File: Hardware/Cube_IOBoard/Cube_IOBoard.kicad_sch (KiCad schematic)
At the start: 15 parts, among them J1 SPKT, J10 Pixhawk_Cube_DF17_Module_Bus_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, J11 GPS1 & I2C1, J12 GPS2 & I2C2, J13 TELEM2, J2 USB, LED & BUZZER, J4 ADC, J5 CAN2, J6 I2C2, J7 TELEM1, J8 CAN1

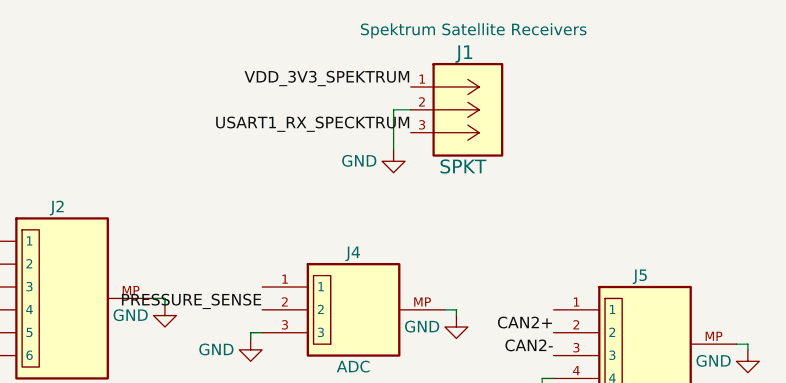
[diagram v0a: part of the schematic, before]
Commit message: Corrected some schematic symbols
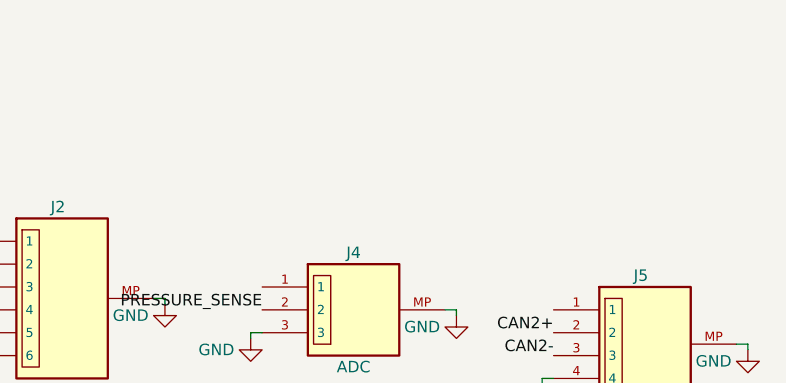
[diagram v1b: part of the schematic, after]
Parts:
- removed J1: SPKT, Connector_JST:JST_XH_B3B-XH-A_1x03_P2.50mm_Vertical, symbol 2022-11-05_21-49-56:S3B-ZR-SM4A-TFLFSN
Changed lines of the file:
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@@
-    (stroke (width 0) (type default) (color 0 0 0 0))
-  )
-  (wire (pts (xy 240.03 26.67) (xy 241.935 26.67))
     (stroke (width 0) (type default) (color 0 0 0 0))
   )
@@
     (stroke (width 0) (type default) (color 0 0 0 0))
   )
-  (wire (pts (xy 240.03 31.115) (xy 240.03 26.67))
-    (stroke (width 0) (type default) (color 0 0 0 0))
-  )
   (wire (pts (xy 224.155 51.435) (xy 224.155 52.07))
     (stroke (width 0) (type default) (color 0 0 0 0))
@@
     (effects (font (size 1.27 1.27)) (justify left bottom))
   )
-  (label "USART1_RX_SPECKTRUM" (at 241.935 29.21 180)
-    (effects (font (size 1.27 1.27)) (justify right bottom))
-  )
   (label "I2C2_SDA" (at 225.425 98.425 180)
     (effects (font (size 1.27 1.27)) (justify right bottom))
@@
   )
   (label "SAFETY" (at 87.63 48.26 180)
-    (effects (font (size 1.27 1.27)) (justify right bottom))
-  )
-  (label "VDD_3V3_SPEKTRUM" (at 241.935 24.13 180)
     (effects (font (size 1.27 1.27)) (justify right bottom))
   )
@@
     )
     (property "Datasheet" "~" (id 3) (at 222.885 136.525 0)
-      (effects (font (size 1.27 1.27)) hide)
-    )
-    (pin "1")
-  )
-  (symbol (lib_id "power:GND") (at 240.03 31.115 0) (unit 1)
-    (in_bom yes) (on_board yes)
-    (property "Reference" "#PWR01" (id 0) (at 240.03 37.465 0)
-      (effects (font (size 1.27 1.27)) hide)
-    )
-    (property "Value" "GND" (id 1) (at 236.22 32.385 0))
-    (property "Footprint" "" (id 2) (at 240.03 31.115 0)
-      (effects (font (size 1.27 1.27)) hide)
-    )
-    (property "Datasheet" "" (id 3) (at 240.03 31.115 0)
       (effects (font (size 1.27 1.27)) hide)
     )
@@
     (pin "1")
   )
-  (symbol (lib_id "2022-11-05_21-49-56:S3B-ZR-SM4A-TFLFSN") (at 239.395 24.13 0) (unit 1)
-    (in_bom yes) (on_board yes)
-    (property "Reference" "J1" (id 0) (at 247.015 20.32 0)
-      (effects (font (size 1.524 1.524)) (justify left))
-    )
-    (property "Value" "SPKT" (id 1) (at 245.11 33.02 0)
-      (effects (font (size 1.524 1.524)) (justify left))
-    )
-    (property "Footprint" "Connector_JST:JST_XH_B3B-XH-A_1x03_P2.50mm_Vertical" (id 2) (at 248.285 21.209 0)
-      (effects (font (size 1.524 1.524)) hide)
-    )
-    (property "Datasheet" "" (id 3) (at 239.395 24.13 0)
-      (effects (font (size 1.524 1.524)))
-    )
-    (property "Description" "Spektrum Satellite Receivers" (id 4) (at 248.92 17.78 0))
-    (pin "1")
-    (pin "2")
-    (pin "3")
-  )
   (symbol (lib_id "BM06B-GHS-TBT_LF__SN__N_:BM06B-GHS-TBT(LF)(SN)(N)") (at 203.2 48.895 0) (unit 1)
     (in_bom yes) (on_board yes)
@@
   )
   (symbol_instances
-    (path "/3dd67373-3ec1-4498-8b23-e797c8947129"
-      (reference "#PWR01") (unit 1) (value "GND") (footprint "")
-    )
     (path "/1dbe8a2e-d3a2-4600-97aa-34c3431dfd48"
       (reference "#PWR02") (unit 1) (value "GND") (footprint "")
@@
       (reference "H4") (unit 1) (value "MountingHole_Pad") (footprint "MountingHole:MountingHole_3.2mm_M3_DIN965_Pad")
     )
-    (path "/b492e4a1-4be3-4440-a10d-9a7c36235ae4"
-      (reference "J1") (unit 1) (value "SPKT") (footprint "Connector_JST:JST_XH_B3B-XH-A_1x03_P2.50mm_Vertical")
-    )
     (path "/b6437e22-8d20-497b-9247-f69a7a68905f"

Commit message: Added EMI filters and TVS to IO schematic, experimenting with spice sims
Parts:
- added C1, C2, C3, C4, C5, C6, C7, C8, C9: KNH16C104DA5TS, libraries:KNH16C104DA5TS, symbol Device:Filter_EMI_C
- added D1, D2, D3, D4, D5, D6, D7, D8, D9: PESD0402-140, Diode_SMD:D_0402_1005Metric, symbol Device:D_TVS
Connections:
- net GND: now also C1.2, C2.2, C3.2, C4.2, C5.2, C6.2, C7.2, C8.2, C9.2, D1.1 (A1), D2.1 (A1), D3.1 (A1), D4.1 (A1), D5.1 (A1), D6.1 (A1), D7.1 (A1), D8.1 (A1), D9.1 (A1)
- net VBUS: now also J10.29 (VBUS); no longer J2.1
- net at J8.1: now also C8.3, D8.2 (A2)
- net at J4.1: now also C1.3, D1.2 (A2)
- net at J6.1: now also C6.3, D5.2 (A2)
- net at J5.1: now also C3.3, D2.2 (A2)
- net at J13.1: now also C9.3, D9.2 (A2)
- net at J12.1: now also C5.3, D6.2 (A2)
- net ~{VDD_5V_PERIPH_EN}: now reaches J10.27 (VDD_5V_PERIPH_EN)
- net ~{VDD_BRICK_VALID}: now reaches J10.55 (VDD_BRICK_VALID)
- net ~{VDD_BACKUP_VALID}: now reaches J10.57 (VDD_BACKUP_VALID)
- net ~{VBUS_VALID}: now reaches J10.59 (VBUS_VALID)
- net VDD_5V_IN_PROT: now reaches J10.61 (VDD_5V_IN_PROT)
- net VDD_5V_IN_PROT: now also J10.63 (VDD_5V_IN_PROT)
- net VDD_SERVO_IN: now reaches J10.9 (VDD_SERVO_IN)
- net at J7.1: now also C4.3, D4.2 (A2)
- net at J11.1: now also C7.3, D7.2 (A2)
- new net: C2.3, D3.2 (A2), J2.1
- new net VDD_5V_HIPOWER: C4.1
- new net VDD_5V_PERIPH: C2.1, C3.1, C5.1, C6.1, C7.1, C8.1, C9.1
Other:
- moved on the sheet: H1, H2, H3, H4, J10, J11, J12, J13, J2, J4, J5, J6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

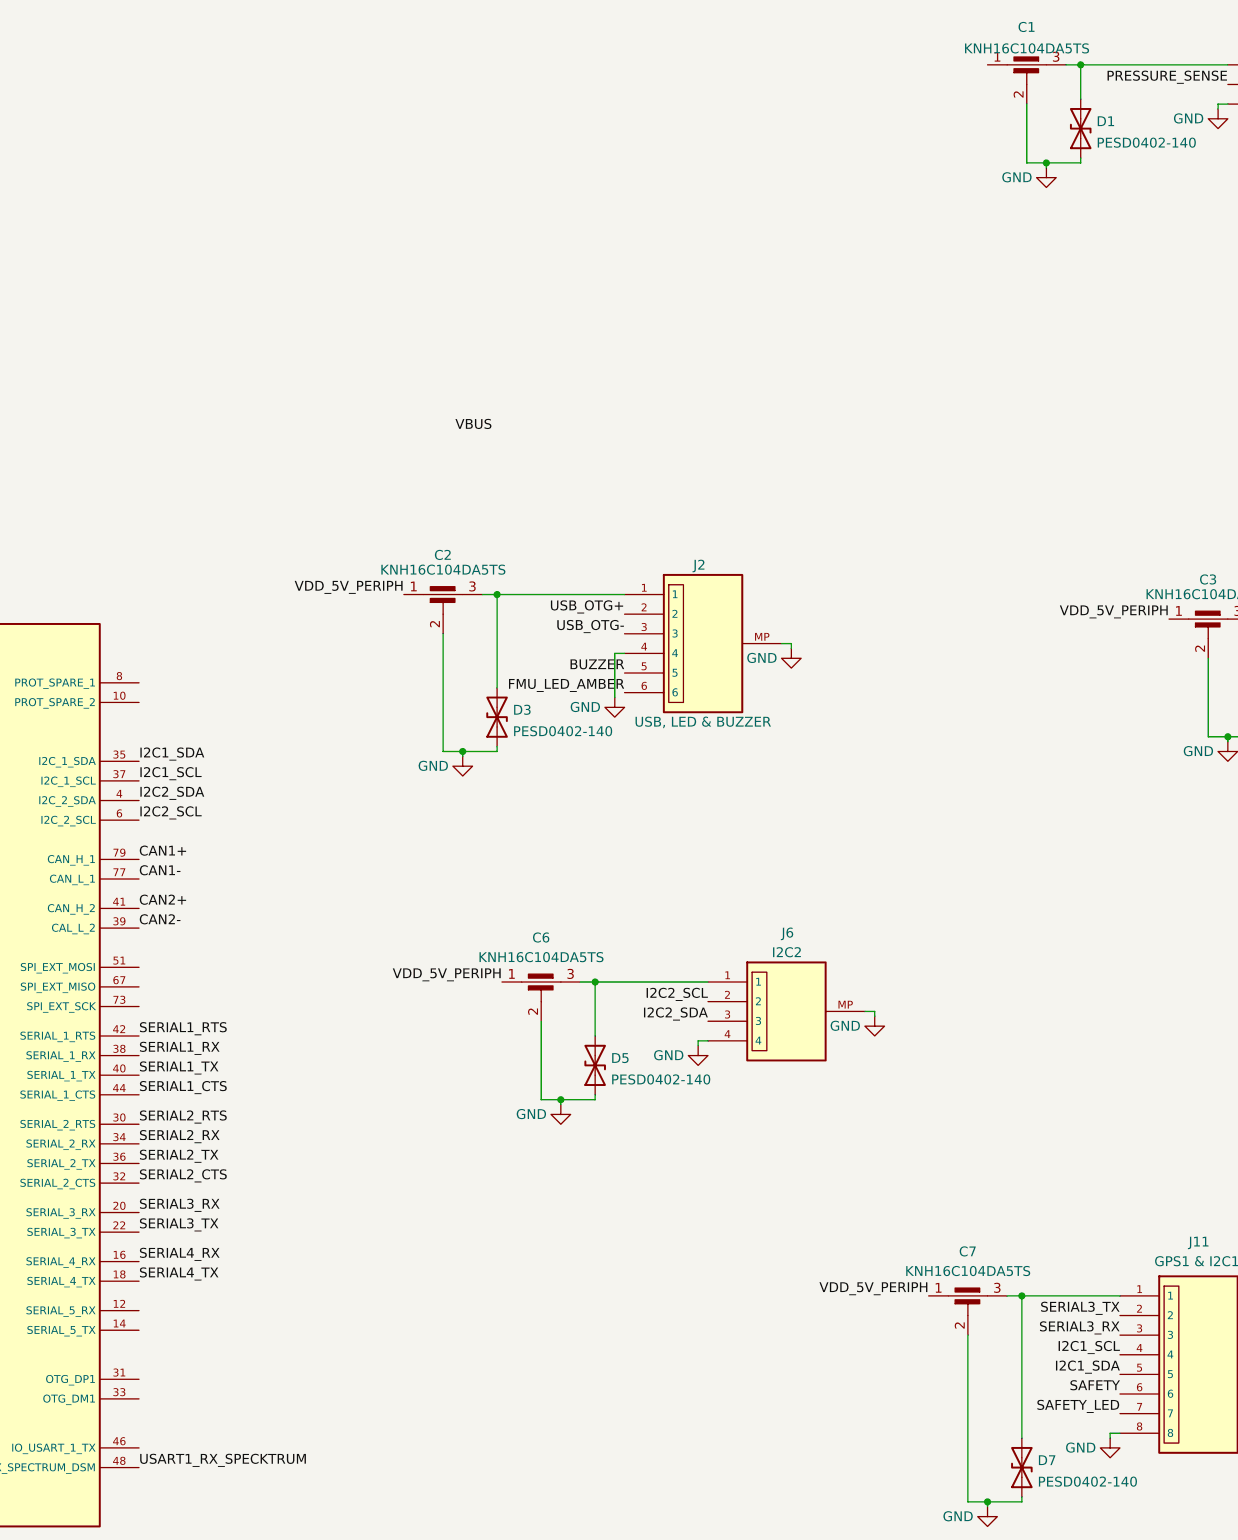
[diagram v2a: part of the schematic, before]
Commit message: Arranged and routed IO connectors
It looks like the VDD 5V Periph is supposed to come from the PSM, either I add pins to connect to a separate module or the entire PSM needs to be implemented on this board...**gulp**
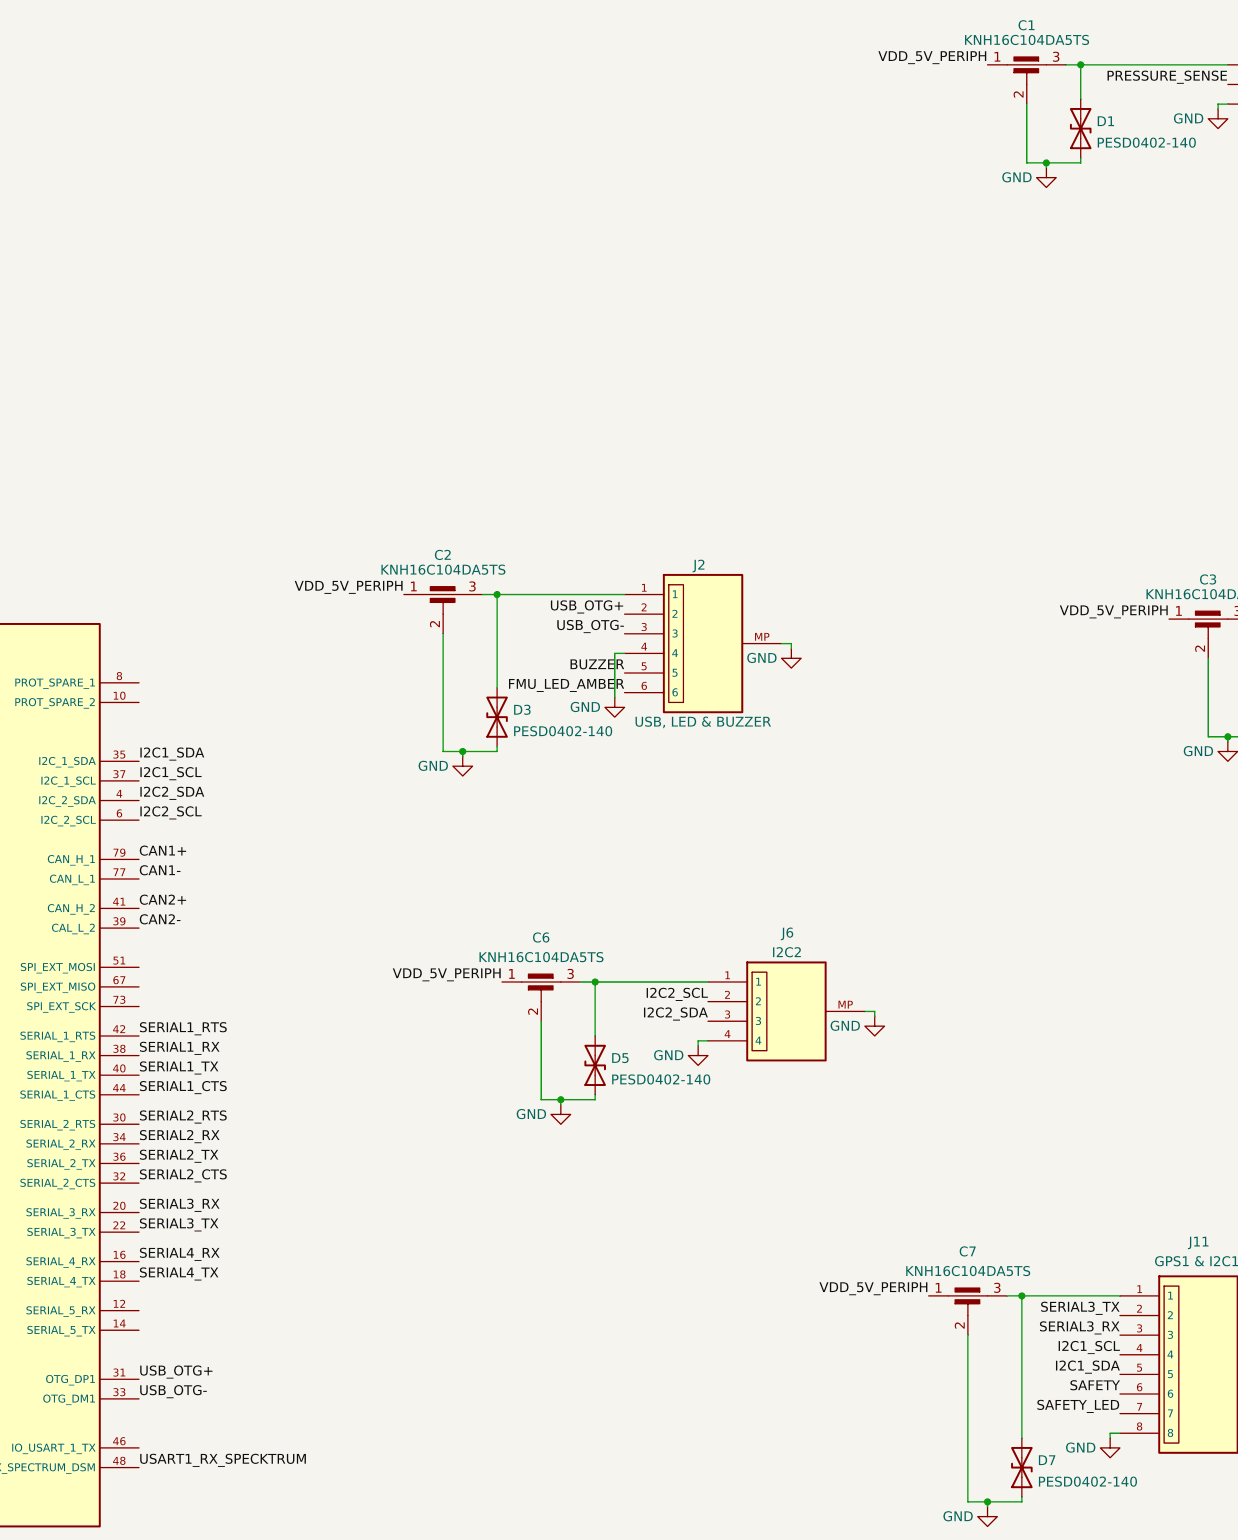
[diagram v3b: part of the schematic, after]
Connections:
- net USB_OTG+: now also J10.31 (OTG_DP1)
- net USB_OTG-: now also J10.33 (OTG_DM1)
- net VDD_5V_PERIPH: now also C1.1
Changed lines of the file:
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@@
+    (effects (font (size 1.27 1.27)) (justify left bottom))
+  )
+  (label "USB_OTG+" (at 100.965 121.92 0)
     (effects (font (size 1.27 1.27)) (justify left bottom))
   )
@@
     (effects (font (size 1.27 1.27)) (justify right bottom))
   )
+  (label "VDD_5V_PERIPH" (at 210.82 -48.26 180)
+    (effects (font (size 1.27 1.27)) (justify right bottom))
+  )
   (label "CAN1-" (at 100.965 57.15 0)
     (effects (font (size 1.27 1.27)) (justify left bottom))
@@
     (effects (font (size 1.27 1.27)) (justify right bottom))
   )
-  (label "VBUS" (at 146.685 -0.635 180)
-    (effects (font (size 1.27 1.27)) (justify right bottom))
+  (label "USB_OTG-" (at 100.965 124.46 0)
+    (effects (font (size 1.27 1.27)) (justify left bottom))
   )
   (label "I2C1_SDA" (at 227.965 121.285 180)
@@
   )
   (symbol (lib_id "Device:Filter_EMI_C") (at 215.9 -45.72 0) (unit 1)
-    (in_bom yes) (on_board yes) (fields_autoplaced)
-    (property "Reference" "C1" (id 0) (at 215.9 -53.1155 0))
-    (property "Value" "KNH16C104DA5TS" (id 1) (at 215.9 -50.3404 0))
+    (in_bom yes) (on_board yes)
+    (property "Reference" "C1" (id 0) (at 215.9 -53.34 0))
+    (property "Value" "KNH16C104DA5TS" (id 1) (at 215.9 -51.435 0))
     (property "Footprint" "libraries:KNH16C104DA5TS" (id 2) (at 215.9 -45.72 90)
       (effects (font (size 1.27 1.27)) hide)
